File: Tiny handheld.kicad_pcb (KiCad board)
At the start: 2 copper layers, 38 parts, among them J1 Conn_01x04_Female, J2 Conn_01x04_Female, J3 TYPE-C-31-M-12, U1 ATtiny85-20P, U2 ATtiny85-20M, U3 EEPROM-I2CEIAJ

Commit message: fixed footprint error U2
Changed the values back to the original
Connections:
- U1 pad 1: PB5/RES -> Net-(U1-Pad1)
- U1 pad 2: PB3 -> Net-(U1-Pad2)
- U1 pad 3: PB4 -> Net-(U1-Pad3)
- U1 pad 5: PB0/SDA/MOSI -> Net-(U1-Pad5)
- U1 pad 6: PB1/MISO -> Net-(U1-Pad6)
- U1 pad 7: PB2/SCL/SCK -> Net-(U1-Pad7)
- U2 pad 1: PB5/RES -> Net-(U1-Pad1)
- U2 pad 11: (no net) -> Net-(U1-Pad5)
- U2 pad 12: (no net) -> Net-(U1-Pad6)
- U2 pad 14: (no net) -> Net-(U1-Pad7)
- U2 pad 15: (no net) -> VCC
- U2 pad 2: PB3 -> Net-(U1-Pad2)
- U2 pad 3: PB4 -> unconnected-(U2-Pad3)
- U2 pad 4: GND -> unconnected-(U2-Pad4)
- U2 pad 5: PB0/SDA/MOSI -> Net-(U1-Pad3)
- U2 pad 6: PB1/MISO -> unconnected-(U2-Pad6)
- U2 pad 7: PB2/SCL/SCK -> unconnected-(U2-Pad7)
- U2 pad 8: VCC -> GND
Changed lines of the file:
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@@
   (net 34 "unconnected-(U2-Pad20)")
   (net 35 "unconnected-(U2-Pad13)")
+  (net 36 "Net-(U1-Pad1)")
+  (net 37 "Net-(U1-Pad2)")
+  (net 38 "Net-(U1-Pad3)")
+  (net 39 "Net-(U1-Pad5)")
+  (net 40 "Net-(U1-Pad6)")
+  (net 41 "Net-(U1-Pad7)")
+  (net 42 "unconnected-(U2-Pad3)")
+  (net 43 "unconnected-(U2-Pad4)")
+  (net 44 "unconnected-(U2-Pad6)")
+  (net 45 "unconnected-(U2-Pad7)")
   (footprint "Jumper:SolderJumper-3_P1.3mm_Open_RoundedPad1.0x1.5mm_NumberLabels" (layer "F.Cu")
     (at 156.9132 41.3976)
@@
     (fp_circle (center -3.005 -1) (end -2.905 -1) (layer "F.Fab") (width 0.2) (fill none))
     (pad "1" smd roundrect locked (at -1.91 -1) (size 0.89 0.26) (layers "F.Cu" "F.Paste" "F.Mask") (roundrect_rratio 0.03)
-      (net 12 "PB5{slash}RES") (pinfunction "~{RESET}/PB5") (pintype "bidirectional"))
+      (net 36 "Net-(U1-Pad1)") (pinfunction "~{RESET}/PB5") (pintype "bidirectional"))
     (pad "2" smd roundrect locked (at -1.91 -0.5) (size 0.89 0.26) (layers "F.Cu" "F.Paste" "F.Mask") (roundrect_rratio 0.03)
-      (net 10 "PB3") (pinfunction "XTAL1/PB3") (pintype "bidirectional"))
+      (net 37 "Net-(U1-Pad2)") (pinfunction "XTAL1/PB3") (pintype "bidirectional"))
     (pad "3" smd roundrect locked (at -1.91 0) (size 0.89 0.26) (layers "F.Cu" "F.Paste" "F.Mask") (roundrect_rratio 0.03)
-      (net 21 "PB4") (pinfunction "XTAL2/PB4") (pintype "bidirectional"))
+      (net 42 "unconnected-(U2-Pad3)") (pinfunction "NC") (pintype "no_connect"))
     (pad "4" smd roundrect locked (at -1.91 0.5) (size 0.89 0.26) (layers "F.Cu" "F.Paste" "F.Mask") (roundrect_rratio 0.03)
+      (net 43 "unconnected-(U2-Pad4)") (pinfunction "NC") (pintype "no_connect"))
+    (pad "5" smd roundrect locked (at -1.91 1) (size 0.89 0.26) (layers "F.Cu" "F.Paste" "F.Mask") (roundrect_rratio 0.03)
+      (net 38 "Net-(U1-Pad3)") (pinfunction "XTAL2/PB4") (pintype "bidirectional"))
+    (pad "6" smd roundrect locked (at -1 1.91 90) (size 0.89 0.26) (layers "F.Cu" "F.Paste" "F.Mask") (roundrect_rratio 0.03)
+      (net 44 "unconnected-(U2-Pad6)") (pinfunction "NC") (pintype "no_connect"))
+    (pad "7" smd roundrect locked (at -0.5 1.91 90) (size 0.89 0.26) (layers "F.Cu" "F.Paste" "F.Mask") (roundrect_rratio 0.03)
+      (net 45 "unconnected-(U2-Pad7)") (pinfunction "NC") (pintype "no_connect"))
+    (pad "8" smd roundrect locked (at 0 1.91 90) (size 0.89 0.26) (layers "F.Cu" "F.Paste" "F.Mask") (roundrect_rratio 0.03)
       (net 1 "GND") (pinfunction "GND") (pintype "power_in"))
-    (pad "5" smd roundrect locked (at -1.91 1) (size 0.89 0.26) (layers "F.Cu" "F.Paste" "F.Mask") (roundrect_rratio 0.03)
-      (net 7 "PB0{slash}SDA{slash}MOSI") (pinfunction "AREF/PB0") (pintype "bidirectional"))
-    (pad "6" smd roundrect locked (at -1 1.91 90) (size 0.89 0.26) (layers "F.Cu" "F.Paste" "F.Mask") (roundrect_rratio 0.03)
-      (net 14 "PB1{slash}MISO") (pinfunction "PB1") (pintype "bidirectional"))
-    (pad "7" smd roundrect locked (at -0.5 1.91 90) (size 0.89 0.26) (layers "F.Cu" "F.Paste" "F.Mask") (roundrect_rratio 0.03)
-      (net 8 "PB2{slash}SCL{slash}SCK") (pinfunction "PB2") (pintype "bidirectional"))
-    (pad "8" smd roundrect locked (at 0 1.91 90) (size 0.89 0.26) (layers "F.Cu" "F.Paste" "F.Mask") (roundrect_rratio 0.03)
-      (net 4 "VCC") (pinfunction "VCC") (pintype "power_in"))
     (pad "9" smd roundrect locked (at 0.5 1.91 90) (size 0.89 0.26) (layers "F.Cu" "F.Paste" "F.Mask") (roundrect_rratio 0.03)
       (net 28 "unconnected-(U2-Pad9)") (pinfunction "NC") (pintype "no_connect"))
     (pad "10" smd roundrect locked (at 1 1.91 90) (size 0.89 0.26) (layers "F.Cu" "F.Paste" "F.Mask") (roundrect_rratio 0.03)
       (net 29 "unconnected-(U2-Pad10)") (pinfunction "NC") (pintype "no_connect"))
-    (pad "11" smd roundrect locked (at 1.91 1) (size 0.89 0.26) (layers "F.Cu" "F.Paste" "F.Mask") (roundrect_rratio 0.03))
-    (pad "12" smd roundrect locked (at 1.91 0.5) (size 0.89 0.26) (layers "F.Cu" "F.Paste" "F.Mask") (roundrect_rratio 0.03))
+    (pad "11" smd roundrect locked (at 1.91 1) (size 0.89 0.26) (layers "F.Cu" "F.Paste" "F.Mask") (roundrect_rratio 0.03)
+      (net 39 "Net-(U1-Pad5)") (pinfunction "AREF/PB0") (pintype "bidirectional"))
+    (pad "12" smd roundrect locked (at 1.91 0.5) (size 0.89 0.26) (layers "F.Cu" "F.Paste" "F.Mask") (roundrect_rratio 0.03)
+      (net 40 "Net-(U1-Pad6)") (pinfunction "PB1") (pintype "bidirectional"))
     (pad "13" smd roundrect locked (at 1.91 0) (size 0.89 0.26) (layers "F.Cu" "F.Paste" "F.Mask") (roundrect_rratio 0.03)
       (net 35 "unconnected-(U2-Pad13)") (pinfunction "NC") (pintype "no_connect"))
-    (pad "14" smd roundrect locked (at 1.91 -0.5) (size 0.89 0.26) (layers "F.Cu" "F.Paste" "F.Mask") (roundrect_rratio 0.03))
-    (pad "15" smd roundrect locked (at 1.91 -1) (size 0.89 0.26) (layers "F.Cu" "F.Paste" "F.Mask") (roundrect_rratio 0.03))
+    (pad "14" smd roundrect locked (at 1.91 -0.5) (size 0.89 0.26) (layers "F.Cu" "F.Paste" "F.Mask") (roundrect_rratio 0.03)
+      (net 41 "Net-(U1-Pad7)") (pinfunction "PB2") (pintype "bidirectional"))
+    (pad "15" smd roundrect locked (at 1.91 -1) (size 0.89 0.26) (layers "F.Cu" "F.Paste" "F.Mask") (roundrect_rratio 0.03)
+      (net 4 "VCC") (pinfunction "VCC") (pintype "power_in"))
     (pad "16" smd roundrect locked (at 1 -1.91 90) (size 0.89 0.26) (layers "F.Cu" "F.Paste" "F.Mask") (roundrect_rratio 0.03)
       (net 30 "unconnected-(U2-Pad16)") (pinfunction "NC") (pintype "no_connect"))
@@
     (fp_line (start 14.3 -3.5) (end 10.64 -3.5) (layer "F.SilkS") (width 0.127))
     (fp_line (start 14.3 3.5) (end 14.3 1.07) (layer "F.SilkS") (width 0.127))
-    (fp_arc (start -10.64 -3.5) (mid -9.50994 -5.917963) (end -7.84 -8) (layer "F.SilkS") (width 0.127))
+    (fp_arc (start -10.64 -3.5) (mid -9.509939 -5.917962) (end -7.84 -8) (layer "F.SilkS") (width 0.127))
     (fp_arc (start 10.64 3.5) (mid 9.50994 5.917963) (end 7.84 8) (layer "F.SilkS") (width 0.127))
     (fp_arc (start 7.84 -8) (mid 9.509972 -5.917983) (end 10.64 -3.5) (layer "F.SilkS") (width 0.127))
-    (fp_arc (start -7.84 8) (mid -9.509972 5.917983) (end -10.64 3.5) (layer "F.SilkS") (width 0.127))
+    (fp_arc (start -7.84 8) (mid -9.509972 5.917982) (end -10.64 3.5) (layer "F.SilkS") (width 0.127))
     (fp_line (start -14.55 8.25) (end -14.55 -8.25) (layer "F.CrtYd") (width 0.05))
     (fp_line (start 14.55 -8.25) (end 14.55 8.25) (layer "F.CrtYd") (width 0.05))
@@
     (fp_line (start 14.3 3.5) (end 10.64 3.5) (layer "F.Fab") (width 0.127))
     (fp_arc (start 10.64 3.5) (mid 9.50994 5.917963) (end 7.84 8) (layer "F.Fab") (width 0.127))
-    (fp_arc (start -7.84 8) (mid -9.509972 5.917983) (end -10.64 3.5) (layer "F.Fab") (width 0.127))
-    (fp_arc (start -10.64 -3.5) (mid -9.50994 -5.917963) (end -7.84 -8) (layer "F.Fab") (width 0.127))
+    (fp_arc (start -7.84 8) (mid -9.509972 5.917982) (end -10.64 3.5) (layer "F.Fab") (width 0.127))
+    (fp_arc (start -10.64 -3.5) (mid -9.509939 -5.917962) (end -7.84 -8) (layer "F.Fab") (width 0.127))
     (fp_arc (start 7.84 -8) (mid 9.509972 -5.917983) (end 10.64 -3.5) (layer "F.Fab") (width 0.127))
     (pad "+" thru_hole circle (at -13.45 -1.27) (size 1.508 1.508) (drill 1) (layers *.Cu *.Mask)
@@
     (fp_line (start 1.635 -1.27) (end 6.985 -1.27) (layer "F.Fab") (width 0.1))
     (pad "1" thru_hole rect (at 0 0) (size 1.6 1.6) (drill 0.8) (layers *.Cu *.Mask)
-      (net 12 "PB5{slash}RES") (pinfunction "~{RESET}/PB5") (pintype "bidirectional"))
+      (net 36 "Net-(U1-Pad1)") (pinfunction "~{RESET}/PB5") (pintype "bidirectional"))
     (pad "2" thru_hole oval (at 0 2.54) (size 1.6 1.6) (drill 0.8) (layers *.Cu *.Mask)
-      (net 10 "PB3") (pinfunction "XTAL1/PB3") (pintype "bidirectional"))
+      (net 37 "Net-(U1-Pad2)") (pinfunction "XTAL1/PB3") (pintype "bidirectional"))
     (pad "3" thru_hole oval (at 0 5.08) (size 1.6 1.6) (drill 0.8) (layers *.Cu *.Mask)
-      (net 21 "PB4") (pinfunction "XTAL2/PB4") (pintype "bidirectional"))
+      (net 38 "Net-(U1-Pad3)") (pinfunction "XTAL2/PB4") (pintype "bidirectional"))
     (pad "4" thru_hole oval (at 0 7.62) (size 1.6 1.6) (drill 0.8) (layers *.Cu *.Mask)
       (net 1 "GND") (pinfunction "GND") (pintype "power_in"))
     (pad "5" thru_hole oval (at 7.62 7.62) (size 1.6 1.6) (drill 0.8) (layers *.Cu *.Mask)
-      (net 7 "PB0{slash}SDA{slash}MOSI") (pinfunction "AREF/PB0") (pintype "bidirectional"))
+      (net 39 "Net-(U1-Pad5)") (pinfunction "AREF/PB0") (pintype "bidirectional"))
     (pad "6" thru_hole oval (at 7.62 5.08) (size 1.6 1.6) (drill 0.8) (layers *.Cu *.Mask)
-      (net 14 "PB1{slash}MISO") (pinfunction "PB1") (pintype "bidirectional"))
+      (net 40 "Net-(U1-Pad6)") (pinfunction "PB1") (pintype "bidirectional"))
     (pad "7" thru_hole oval (at 7.62 2.54) (size 1.6 1.6) (drill 0.8) (layers *.Cu *.Mask)
-      (net 8 "PB2{slash}SCL{slash}SCK") (pinfunction "PB2") (pintype "bidirectional"))
+      (net 41 "Net-(U1-Pad7)") (pinfunction "PB2") (pintype "bidirectional"))
     (pad "8" thru_hole oval (at 7.62 0) (size 1.6 1.6) (drill 0.8) (layers *.Cu *.Mask)
       (net 4 "VCC") (pinfunction "VCC") (pintype "power_in"))

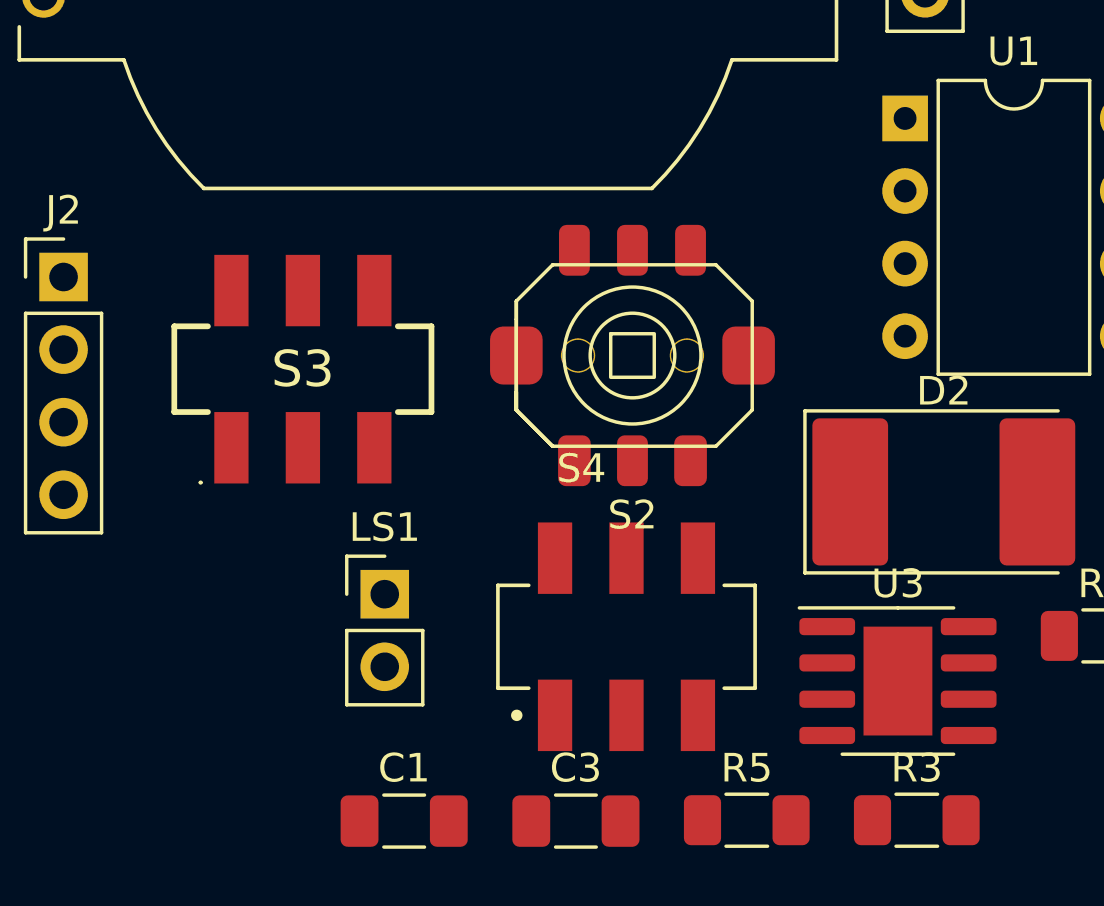
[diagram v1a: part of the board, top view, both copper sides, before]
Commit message: removed all errors from pcb new
Ready to start pcb design
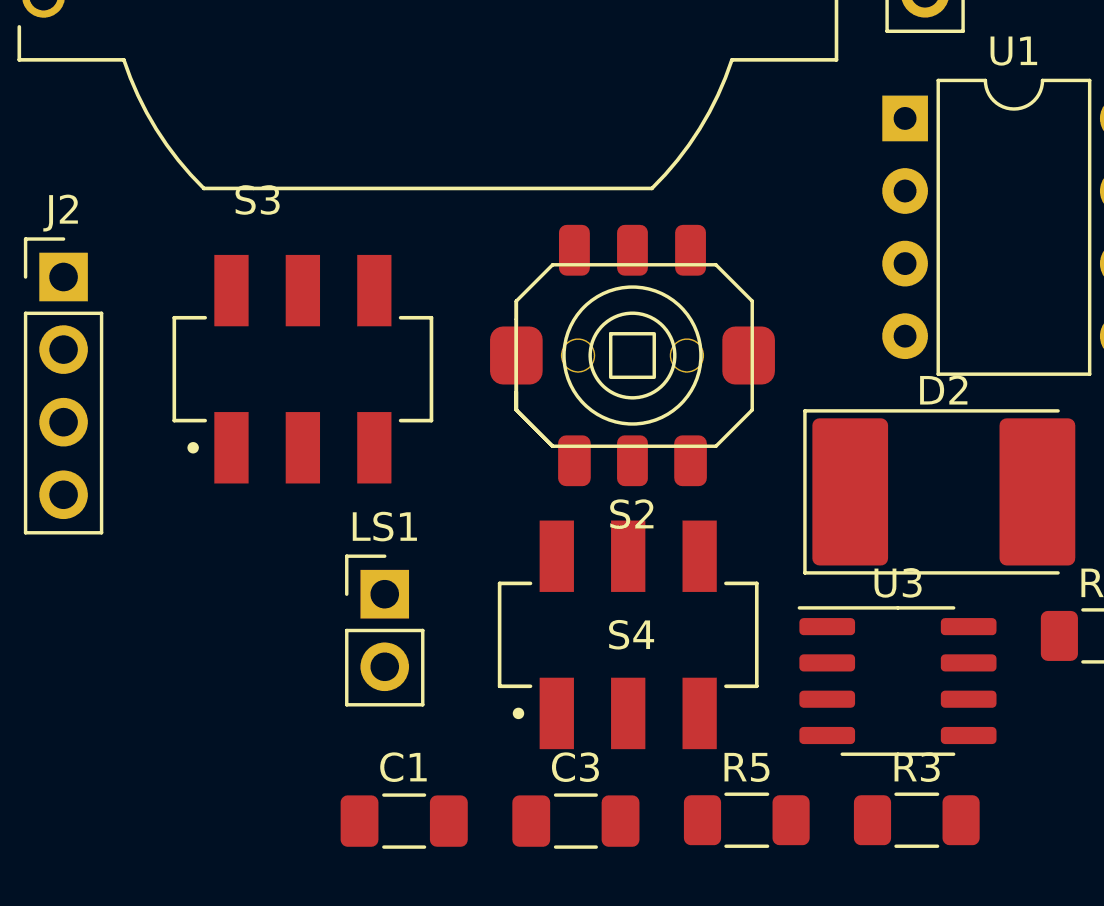
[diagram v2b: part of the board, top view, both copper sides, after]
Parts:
- S3: footprint SmacSYs:JS202011SCQN -> Snapeda:SW_JS202011SCQN
- S4: value SWITCH-SP3T-SMD -> JS202011SCQN
- U3: footprint Package_SO:SOIC-8-1EP_3.9x4.9mm_P1.27mm_EP2.41x3.81mm -> Package_SO:SOIC-8_3.9x4.9mm_P1.27mm
- moved S4 0.09 mm to (112.6, 65.4)
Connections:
- S2 pad 7: (no net) -> GND
- S2 pad 8: (no net) -> GND
- S4 pad 1: Net-(LS1-Pad1) -> unconnected-(S4-Pad1)
- S4 pad 2: Net-(LS1-Pad1) -> unconnected-(S4-Pad2)
- S4 pad 3: GND -> unconnected-(S4-Pad3)
- S4 pad 5: (no net) -> Net-(LS1-Pad1)
- S4 pad 6: (no net) -> Net-(LS1-Pad1)

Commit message: changed speaker footprint and updated it
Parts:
- LS1: value Speaker -> KSSGK4B16-20; footprint Connector_PinHeader_2.54mm:PinHeader_1x02_P2.54mm_Vertical -> Snapeda:XDCR_KSSGK4B16-20
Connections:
- S4 pad 5: Net-(LS1-Pad1) -> Net-(S4-Pad5)
- S4 pad 6: Net-(LS1-Pad1) -> Net-(S4-Pad5)

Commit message: first layout tryout
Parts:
- removed J2: Conn_01x04_Female, Connector_PinHeader_2.54mm:PinHeader_1x04_P2.54mm_Vertical
- BT1, JP1, JP2, JP3, JP4, LS1, S4: moved to B.Cu
- D1, D2, D3: footprint Diode_SMD:D_3220_8050Metric_Pad2.65x5.15mm_HandSolder -> Diode_SMD:D_1210_3225Metric_Pad1.42x2.65mm_HandSolder
- moved J3 91.3 mm to (167.6, 128.3)
- moved S3 90.4 mm to (177.8, 104.1), turned to 90 degrees
- moved JP2 86.2 mm to (180.3, 125.7), turned to 180 degrees
- moved LS1 83.5 mm to (167.6, 118.1), turned to 180 degrees
- moved JP3 82.7 mm to (175.3, 125.7), turned to 180 degrees
- moved JP1 82.6 mm to (180.3, 120.7), turned to 180 degrees
- moved S1 82.5 mm to (177.8, 114.3)
- moved D3 77.0 mm to (180.3, 95.2)
- moved JP4 73.4 mm to (175.3, 120.7), turned to 180 degrees
- moved BT1 71.0 mm to (158.8, 88.9), turned to -90 degrees
- moved U1 70.4 mm to (163.8, 104.2)
- moved U2 68.9 mm to (167.6, 108.0)
- moved U3 68.5 mm to (167.6, 118.1)
- moved S2 68.1 mm to (156.1, 110.8), turned to 90 degrees
- moved S4 67.0 mm to (178.4, 78.1), turned to 180 degrees
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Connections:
- S2 pad 7: GND -> (no net)
- S2 pad 8: GND -> (no net)
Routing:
- net (no net): vias 0 -> 1
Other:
- board outline added: 34.3 x 58.4 mm

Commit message: layout improved
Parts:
- C1, C2, C3, C4, C5, D1, D2, D3, R1, R10, R11, R12, R13, R14, R2, R3, R4, R5, R6, R7, R8, R9, U3: moved to B.Cu
- JP1, JP2, JP3, JP4: moved to F.Cu
- moved R3 35.3 mm to (181.6, 116.8), turned to 180 degrees
- moved JP4 29.2 mm to (154.9, 99.7), turned to 0 degrees
- moved R10 29.1 mm to (181.8, 105.4), turned to 180 degrees
- moved R12 29.1 mm to (181.8, 101.6), turned to 180 degrees
- moved R11 28.9 mm to (175.3, 109.2), turned to 180 degrees
- moved R6 28.9 mm to (175.3, 105.4), turned to 180 degrees
- moved R1 28.9 mm to (175.2, 113.0), turned to 180 degrees
- moved R5 28.9 mm to (175.2, 116.8), turned to 180 degrees
- moved R2 28.8 mm to (175.3, 101.6), turned to 180 degrees
- moved JP3 28.7 mm to (163.2, 99.7), turned to 0 degrees
- moved R7 28.4 mm to (181.6, 113.0), turned to 180 degrees
- moved JP2 27.5 mm to (171.4, 99.7), turned to 0 degrees
- moved JP1 21.0 mm to (179.1, 99.7), turned to 0 degrees
- moved R8 19.3 mm to (181.6, 109.2), turned to 180 degrees
- moved S3 16.8 mm to (167.6, 117.5), turned to 180 degrees
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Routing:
- net (no net): vias 1 -> 2

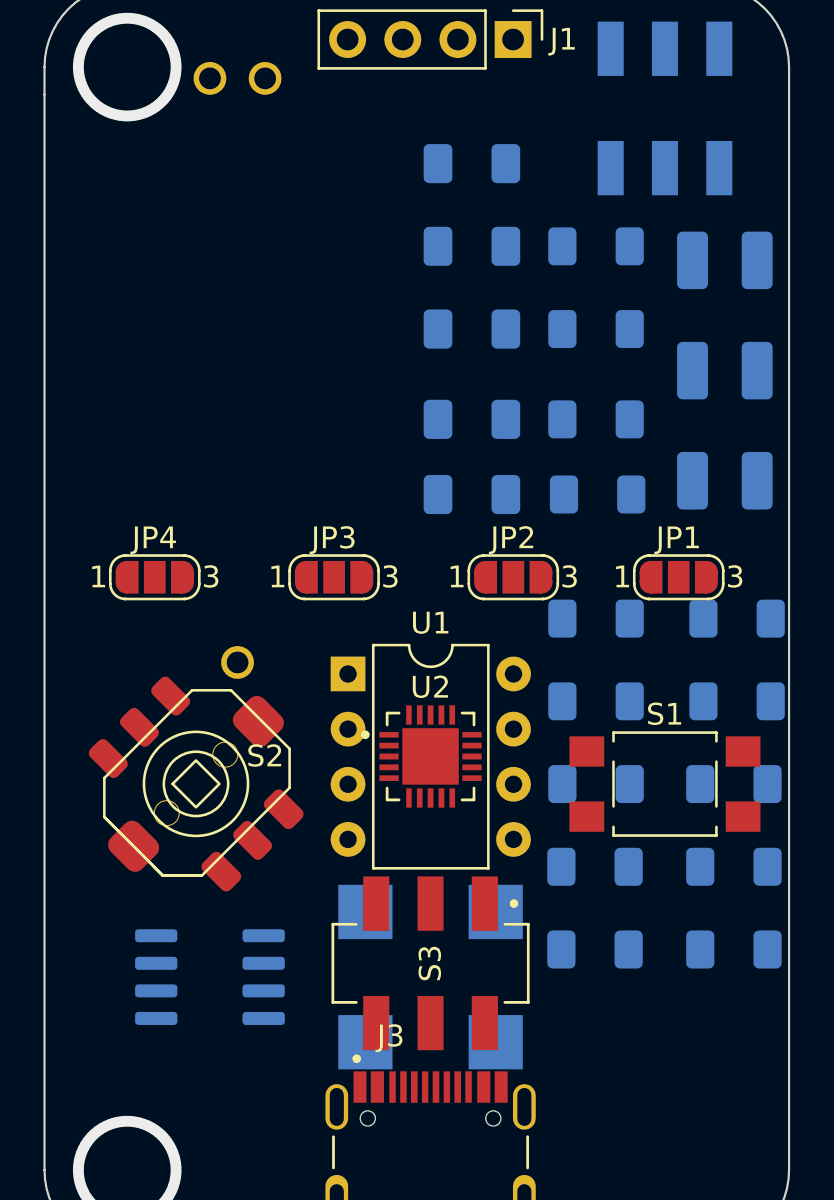
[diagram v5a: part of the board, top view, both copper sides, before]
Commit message: improved layout and added silkscreen
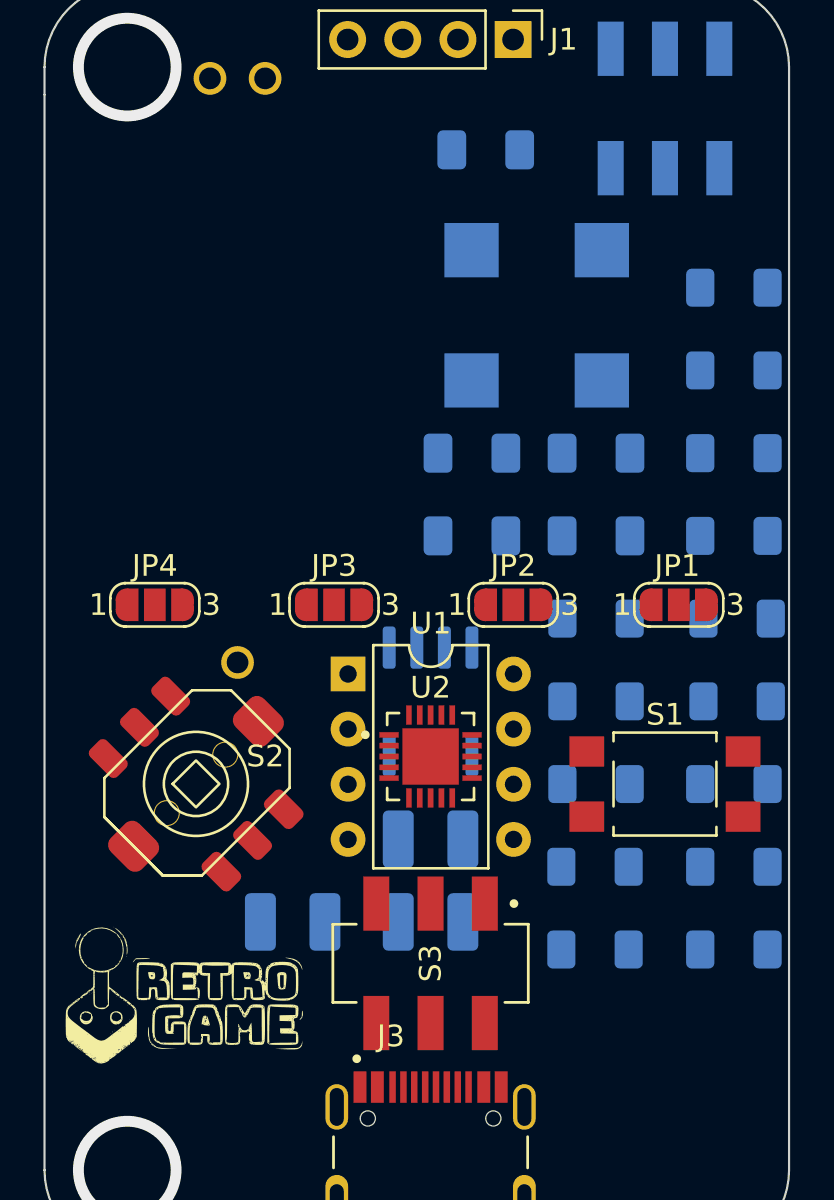
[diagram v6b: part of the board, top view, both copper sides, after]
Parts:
- added G***: LOGO, Libraries:logo retro, F.Cu at (156.3, 119.1)
- moved D2 32.3 mm to (161.3, 115.6)
- moved LS1 30.9 mm to (172.5, 87.6)
- moved D1 29.9 mm to (167.6, 111.8)
- moved D3 24.4 mm to (167.6, 115.6)
- moved U3 16.3 mm to (167.6, 105.4), turned to -90 degrees
- moved C2 14.5 mm to (175.3, 94.0)
- moved C4 14.5 mm to (175.3, 97.8)
- moved R13 11.4 mm to (181.6, 97.8)
- moved R14 11.4 mm to (181.6, 94.0)
- moved R9 8.78 mm to (181.6, 86.4)
- moved R4 8.49 mm to (181.6, 90.2)
- moved C5 8.28 mm to (170.2, 80.0)
- moved C1 1.91 mm to (169.5, 97.8)
- moved C3 1.56 mm to (169.5, 94.0)
- moved JP1 1.27 mm to (179.1, 101.0)
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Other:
- board text added: "5V usb"
- board text added: "CR2032 Battery"
- board text added: "EEPROM"
- board text added: "Tiny Handheld Casper R. Tak"
